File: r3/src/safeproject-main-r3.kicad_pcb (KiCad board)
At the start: 4 copper layers, 57.3 x 109 mm, 173 parts, among them J1 , J10 502443-0560, J11 SMA, J12 U_FL-R-SMT-1_10_, J13 JAE_SIM_Card_SF72S006, J14 Micro_SD_Card_Det_JAE_ST11, J15 10118194, J16 FH12A-20S-0.5SH, J2 , J3 , J4 , J5 , J6 , J7 , J8 , J9 , Q1 Si7113ADN, Q10 NX3008NBKW, Q11 NX3008NBKW, Q2 Si7113ADN, Q3 Si7113ADN, Q4 NX3008NBKW, Q5 NX3008NBKW, Q6 NX3008NBKW, Q7 NX3008NBKW, Q8 NX3008NBKW, Q9 NX3008NBKW, T1 , T10 , T11 , T12 , T13 , T14 , T15 , T16 , T2 , T3 , T4 , T5 , T6 , T7 , T8 , T9 , U1 74LVC1G07DCK, U10 ESD7004, U11 ESD7004, U12 CP2102N-Axx-xQFN24, U13 DS3231MZ, U14 74LVC1G07DCK, U15 FSUSB42MX, U16 ESD7004, U2 ESD7004, U3 DZDH0401DW, U4 DZDH0401DW, U5 LM60440DRPK, U6 LM60440DRPK, U7 Sierra_Wireless_RC7620, U8 ESD7004, U9 PCF8574PW

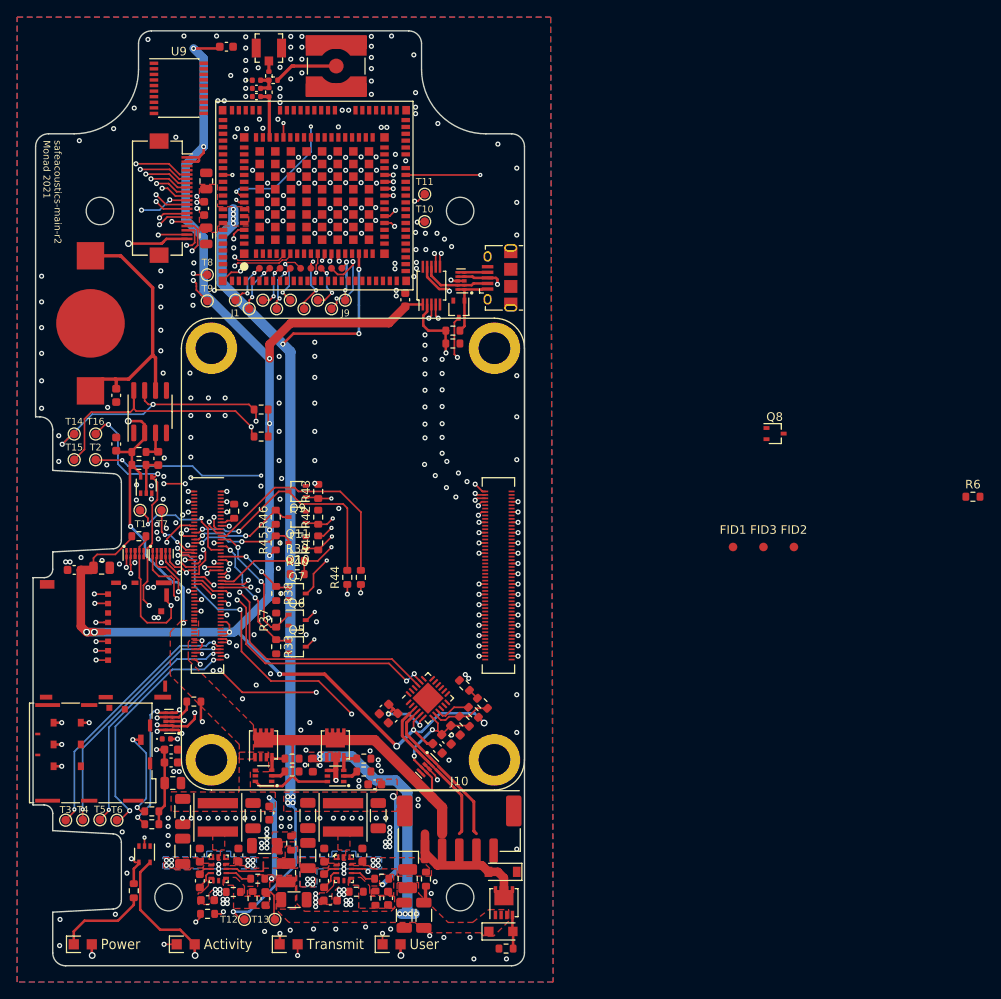
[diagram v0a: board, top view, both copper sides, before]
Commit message: LED driver routed
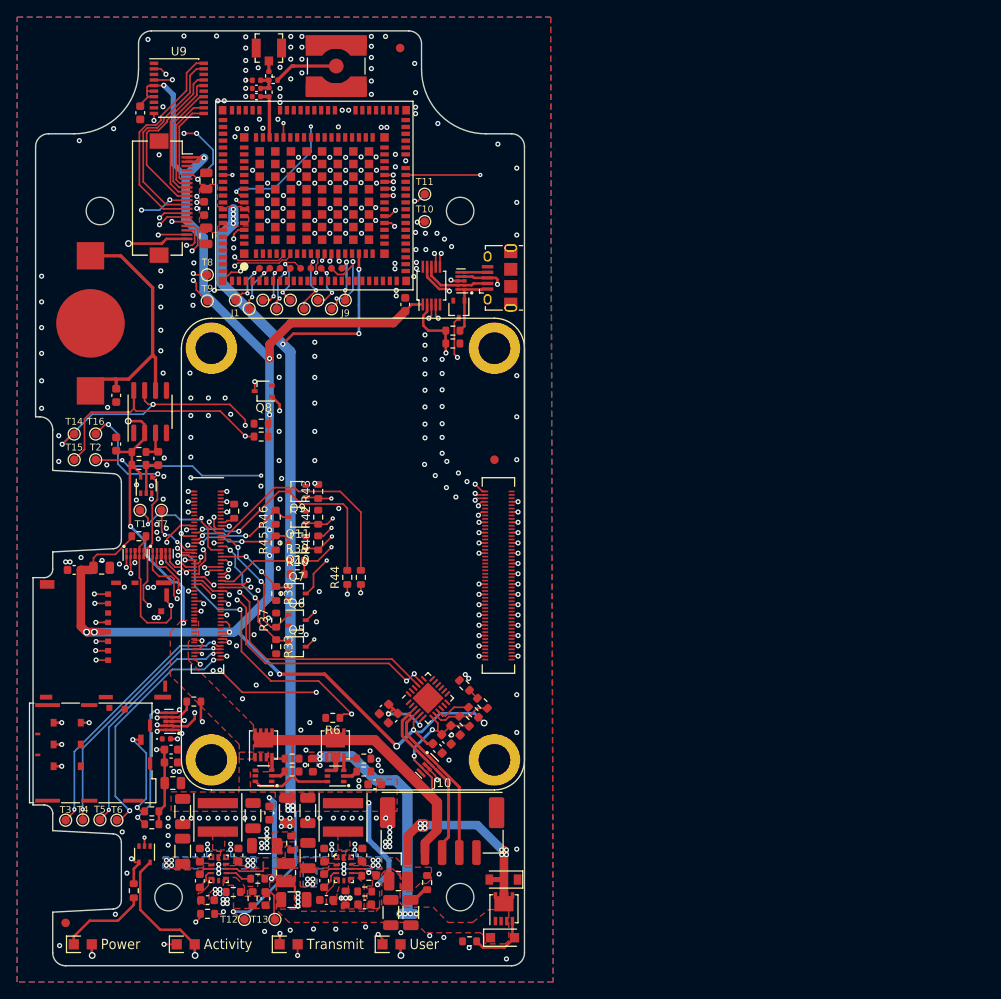
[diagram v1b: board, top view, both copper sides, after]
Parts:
- moved FID2 95.6 mm to (-25.0, 43.0)
- moved R6 79.0 mm to (6.15, 19.1), turned to 180 degrees
- moved FID1 69.9 mm to (14.0, -59.0)
- moved Q8 59.9 mm to (-1.95, -19.0), turned to 180 degrees
- moved FID3 33.0 mm to (25.0, -11.0)
- moved C38 12.7 mm to (-16.3, -51.5), turned to 90 degrees
- moved C14 10.6 mm to (0.85, 29.9)
- moved R11 4.33 mm to (22.1, 45.1)
- moved C12 2.82 mm to (9.87, 40.9), turned to 180 degrees
- moved J10 2.01 mm to (18.9, 32.3)
- moved R2 1.65 mm to (-2.20, -15.2)
- moved C43 1.59 mm to (12.9, 41.8)
- moved C45 1.55 mm to (15.2, 41.8)
- moved R13 1.54 mm to (10.3, 37.5)
- moved R16 1.48 mm to (9.87, 39.3), turned to 180 degrees
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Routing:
- net unconnected-(Module1-Pad44): track 79.3 -> 0.00 mm, vias 4 -> 0
- net Net-(D6-Pad2): track 91.4 -> 65.6 mm
- net /Power and input connector/IN_VIN: track 0.00 -> 23.3 mm, vias 0 -> 8
- net /Modem/UIM_SIM_DET: track 0.00 -> 21.5 mm, vias 0 -> 2
- net VBUS: track 72.3 -> 59.8 mm
- net /LED driver, LED board connections/LED3_B: track 13.4 -> 25.2 mm, vias 1 -> 0
- net /LED driver, LED board connections/LED3_G: track 14.1 -> 23.4 mm, vias 1 -> 0
- net /LED driver, LED board connections/LED1_G: track 17.9 -> 10.4 mm, vias 1 -> 0
- net /LED driver, LED board connections/LED2_B: track 12.9 -> 19.9 mm, vias 1 -> 0
- net /LED driver, LED board connections/LED1_B: track 16.6 -> 11.8 mm, vias 1 -> 0
- net /LED driver, LED board connections/LED1_R: track 18.9 -> 14.8 mm, vias 1 -> 4
- net Net-(D5-Pad2): track 3.95 -> 7.21 mm
- net /SDA: track 107.6 -> 105.4 mm, vias 5 -> 6
- net /LED driver, LED board connections/LED2_R: track 15.4 -> 13.5 mm, vias 1 -> 0
- net /3V7_EN: track 55.5 -> 57.4 mm
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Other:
- board text added: "bugg-main-r3 Monad 2021"
- board text removed: "safeacoustics-main-r2 Monad 2021"

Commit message: All nets routed
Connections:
- J13 pad C7: /Modem/UIM_CLK -> /Modem/UIM_DATA
- R22 pad 1: /Modem/UIM_CLK -> /Modem/UIM_DATA
- U7 pad 28: /Modem/UIM_CLK -> /Modem/UIM_DATA
- U8 pad 5: /Modem/UIM_CLK -> /Modem/UIM_DATA
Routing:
- net /Modem/UIM_DATA: track 0.00 -> 107.6 mm, vias 0 -> 5
- net /Modem/UIM_CLK: track 187.1 -> 79.5 mm, vias 7 -> 2
- net /SDA: track 105.4 -> 106.6 mm

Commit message: Create a variant of the pi without holes, so they don't interfere with the Wurth spacer holes. Fix the mounting holes to create bare FR4 regions as in r2. New variant of the spacers with connectable pads. Spacers are connected to GND plane
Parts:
- Module1: footprint Raspberry_Pi_CM4:Raspberry-Pi-4-Compute-Module -> jeffmakes-footprints:Raspberry-Pi-4-Compute-Module-no-holes
